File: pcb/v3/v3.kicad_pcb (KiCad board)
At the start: 2 copper layers, 100 x 100 mm, 50 parts, among them J1 RJ10, J10 USB_A, J2 ICSP, J3 RJ10, J4 RJ10, J5 RJ10, J6 RJ10, J7 RJ10, J8 BOOST, J9 USB_B, Q1 BS170, Q2 2N3904, Q3 BS170, SW1 CTL1, SW2 CTL2, SW3 CTL3, U1 ATmega328P-PU, U2 PCF8574, U3 RC1602A, Y1 16MHz

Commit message: v3: initial component placement
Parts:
- C1, C2, C3, C4, C5, C6: footprint Capacitor_THT:C_Disc_D3.8mm_W2.6mm_P2.50mm -> Capacitor_SMD:C_1206_3216Metric_Pad1.42x1.75mm_HandSolder
- J2: footprint kamaji:ATmega_ISP_6pin -> Connector_IDC:IDC-Header_2x05_P2.54mm_Horizontal
- R1, R10, R11, R12, R13, R18, R19, R2, R3, R5, R6, R7, R8, R9: footprint Resistor_THT:R_Axial_DIN0207_L6.3mm_D2.5mm_P10.16mm_Horizontal -> Resistor_SMD:R_1206_3216Metric_Pad1.42x1.75mm_HandSolder
- SW1, SW2, SW3, U3: moved to B.Cu
- moved JP1 362.5 mm to (65.3, 122.5)
- moved J4 339.2 mm to (61.5, 46.0), turned to 180 degrees
- moved SW1 338.0 mm to (70.0, 140.0)
- moved J10 336.3 mm to (59.0, 86.0), turned to 270 degrees
- moved JP2 333.8 mm to (61.8, 125.0), turned to 180 degrees
- moved J6 326.7 mm to (76.0, 46.0), turned to 180 degrees
- moved J3 321.2 mm to (90.5, 46.0), turned to 180 degrees
- moved Q1 310.0 mm to (115.8, 115.5)
- moved J7 309.1 mm to (105.0, 46.0), turned to 180 degrees
- moved LS1 297.3 mm to (79.8, 111.2)
- moved J5 296.1 mm to (119.5, 46.0), turned to 180 degrees
- moved Q3 290.9 mm to (64.5, 93.0)
- moved R4 287.3 mm to (85.5, 82.5), turned to 270 degrees
- moved J8 278.7 mm to (115.8, 126.8), turned to 90 degrees
- moved U1 275.5 mm to (91.0, 91.5), turned to 90 degrees
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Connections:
- J2 pad 1: /CBTN2 -> /CBTN1
- J2 pad 3: /CBTN3 -> (no net)
- J2 pad 4: /CBTN1 -> GND
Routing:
- added copper zone on B.Cu, net GND
- added copper zone on F.Cu, net GND

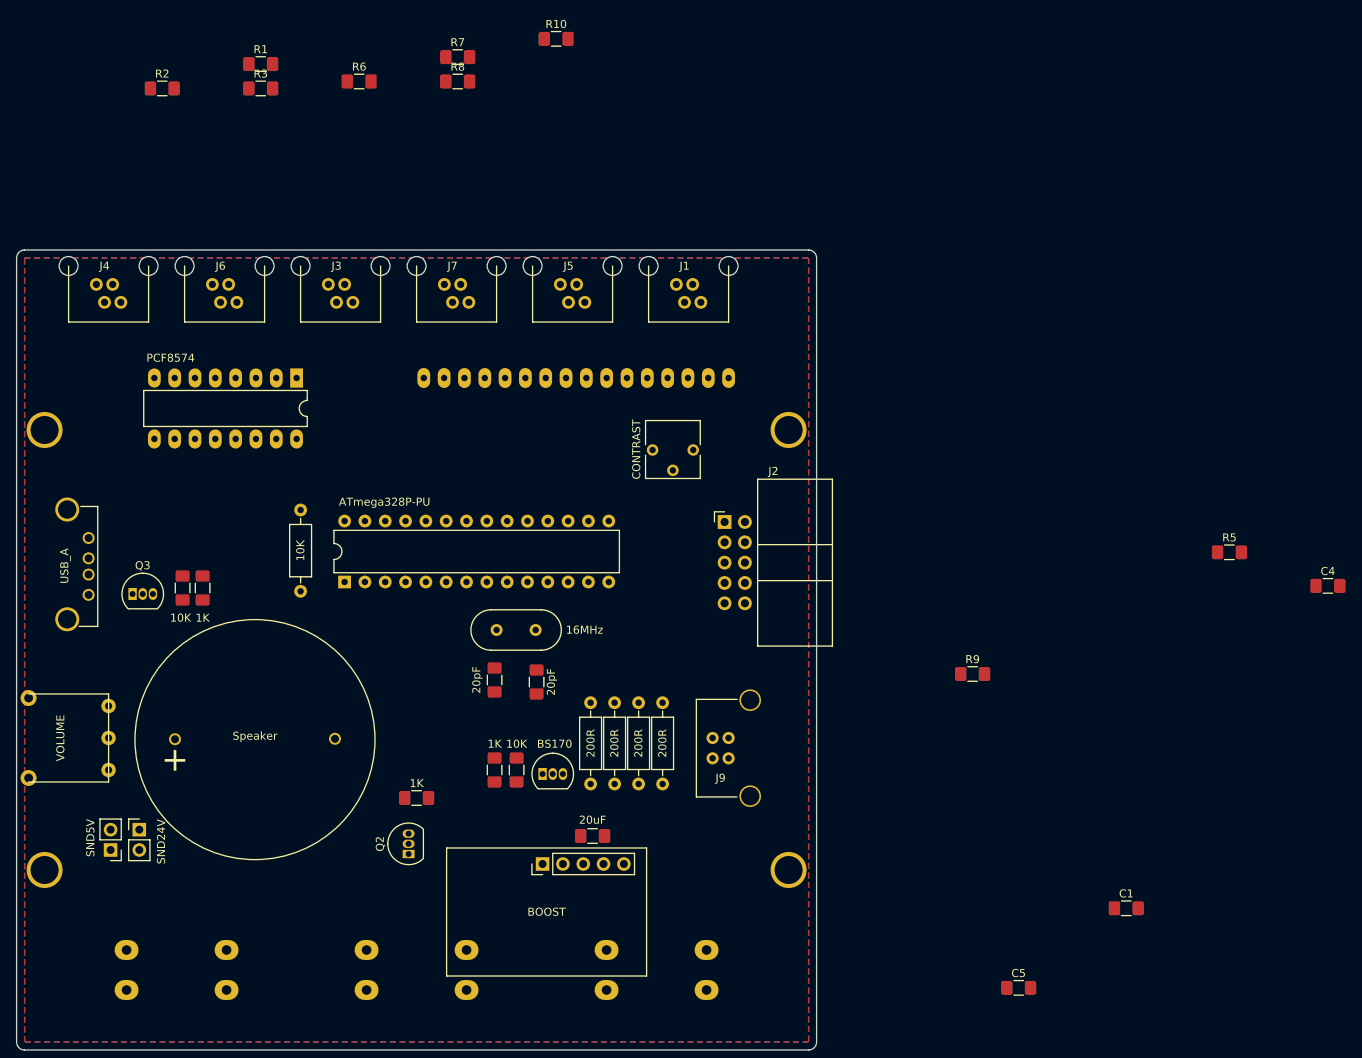
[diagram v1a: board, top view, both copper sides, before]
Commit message: v3: move components around
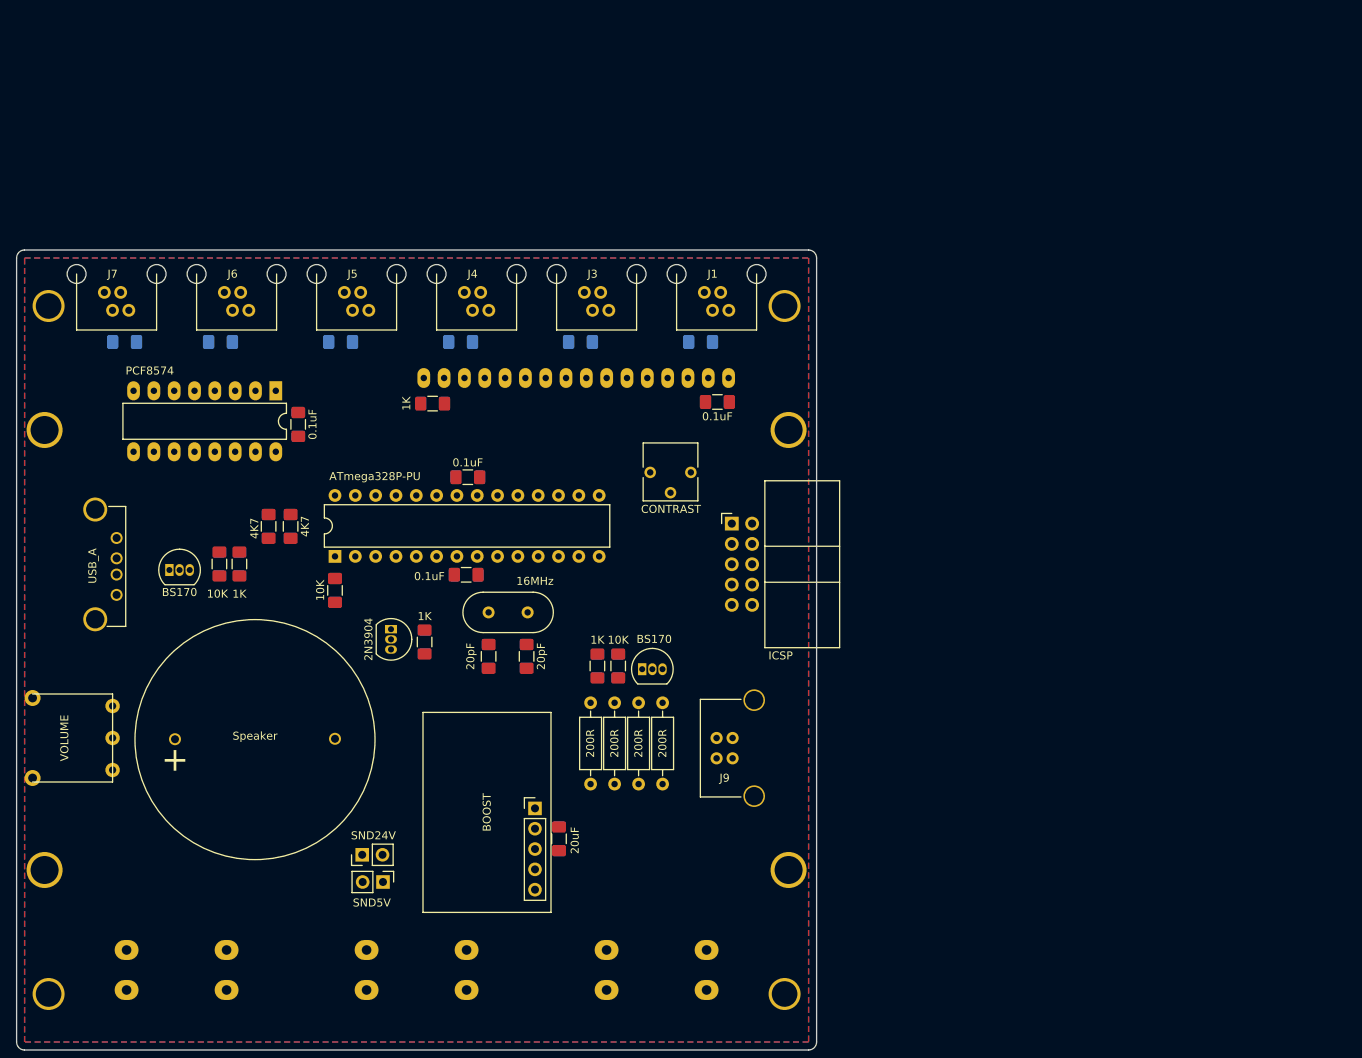
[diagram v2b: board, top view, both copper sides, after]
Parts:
- added C7: 0.1uF, Capacitor_SMD:C_1206_3216Metric_Pad1.42x1.75mm_HandSolder, F.Cu at (106.2, 90.6)
- added REF**: 1pin, kamaji:Drill_Hole_M3, F.Cu at (54.0, 143.0)
- added REF**: 1pin, kamaji:Drill_Hole_M3, F.Cu at (146.0, 57.0)
- added REF**: 1pin, kamaji:Drill_Hole_M3, F.Cu at (146.0, 143.0)
- added REF**: 1pin, kamaji:Drill_Hole_M3, F.Cu at (54.0, 57.0)
- R1, R2, R3, R5, R8, R9: moved to B.Cu
- R4: footprint Resistor_THT:R_Axial_DIN0207_L6.3mm_D2.5mm_P10.16mm_Horizontal -> Resistor_SMD:R_1206_3216Metric_Pad1.42x1.75mm_HandSolder
- moved C4 130.3 mm to (85.2, 71.8), turned to 90 degrees
- moved R5 114.2 mm to (90.5, 61.5), turned to 180 degrees
- moved R9 113.8 mm to (63.5, 61.5)
- moved C5 93.9 mm to (106.4, 78.4), turned to 180 degrees
- moved C1 81.3 mm to (137.6, 69.0)
- moved R1 65.0 mm to (135.5, 61.5), turned to 180 degrees
- moved R7 63.2 mm to (81.5, 84.5), turned to 90 degrees
- moved R2 61.1 mm to (120.5, 61.5), turned to 180 degrees
- moved R6 56.3 mm to (84.2, 84.5), turned to 90 degrees
- moved R10 48.1 mm to (102.0, 69.2), turned to 180 degrees
- moved J4 46.0 mm to (107.5, 47.0)
- moved R8 44.0 mm to (75.5, 61.5), turned to 180 degrees
- moved J7 42.5 mm to (62.5, 47.0)
- moved R3 40.4 mm to (105.5, 61.5), turned to 180 degrees
- moved JP2 34.3 mm to (95.8, 129.0), turned to 270 degrees
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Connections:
- J2 pad 1: /CBTN1 -> /CBTN3
- J2 pad 7: /CBTN3 -> /CBTN1
- U1 pad 11: /PBTN6 -> /PBTN1
- U1 pad 17: /CBTN1 -> /CBTN3
- U1 pad 19: /CBTN3 -> /CBTN1
- U1 pad 2: /PBTN1 -> /PBTN6
- U1 pad 3: /PBTN2 -> /PBTN5
- U1 pad 4: /PBTN3 -> /PBTN4
- U1 pad 5: /PBTN4 -> /PBTN3
- U1 pad 6: /PBTN5 -> /PBTN2

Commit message: v3: finish layout
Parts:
- Q1, Q2, Q3: footprint Package_TO_SOT_THT:TO-92_Inline -> Package_TO_SOT_THT:TO-92_Inline_Wide
- moved R6 5.42 mm to (80.0, 81.2)
- moved R7 5.42 mm to (77.2, 81.2)
- moved RV2 4.00 mm to (56.0, 115.0)
- moved Q3 3.58 mm to (70.5, 93.3), turned to 90 degrees
- moved Q1 2.06 mm to (129.2, 104.2), turned to 90 degrees
- moved R4 1.83 mm to (88.3, 91.5), turned to 0 degrees
- moved Q2 0.50 mm to (96.8, 97.9)
- moved R11 0.50 mm to (122.1, 102.0)
- moved R13 0.50 mm to (124.7, 102.0)
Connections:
- J2 pad 1: /CBTN3 -> /CBTN1
- J2 pad 7: /CBTN1 -> /CBTN2
- J2 pad 9: /CBTN2 -> /CBTN3
- U1 pad 12: /LCDRS -> /LCDE
- U1 pad 13: /LCDE -> /LCDRS
- U1 pad 17: /CBTN3 -> /CBTN1
- U1 pad 18: /CBTN2 -> /CBTN3
- U1 pad 19: /CBTN1 -> /CBTN2
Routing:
- net VCC: track 0.00 -> 287.9 mm, vias 0 -> 4
- net /CBTN1: track 0.00 -> 139.0 mm
- net /CBTN2: track 0.00 -> 109.3 mm
- net /CBTN3: track 0.00 -> 97.0 mm
- net /RST: track 0.00 -> 62.5 mm
- net /PLED1: track 0.00 -> 62.0 mm
- net /PLED2: track 0.00 -> 49.5 mm
- net /PBTN6: track 0.00 -> 48.9 mm
- net /LAMP: track 0.00 -> 46.4 mm, vias 0 -> 1
- net /PBTN1: track 0.00 -> 45.3 mm
- net /PBTN2: track 0.00 -> 40.6 mm
- net /PBTN3: track 0.00 -> 37.6 mm
- net Net-(JP1-Pad1): track 0.00 -> 37.4 mm
- net /PBTN5: track 0.00 -> 37.3 mm
- net /PLED3: track 0.00 -> 37.1 mm
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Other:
- net class Power added: clearance 0.25, trace_width 0.5, via_dia 0.8, via_drill 0.4
- board text added: "Kamaji 3.0 github.com/iley/kamaji"

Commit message: v3: minor layout improvements
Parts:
- moved RV2 5.00 mm to (56.0, 110.0)
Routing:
- net Net-(JP1-Pad1): track 37.4 -> 39.4 mm
- net Net-(LS1-Pad1): track 9.39 -> 8.28 mm
- net /PBTN2: track 40.6 -> 39.7 mm
- net VCC: track 287.9 -> 287.3 mm
